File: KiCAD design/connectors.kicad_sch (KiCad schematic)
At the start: 8 parts, among them J201 Conn_02x19_Odd_Even, J202 Conn_01x03_Female, J203 Conn_01x03_Female, J204 Conn_02x19_Odd_Even, J205 JST BATTERY, J206 JST SENS TOF 2, J207 Conn_01x06_Female, J208 JST SENS TOF 1

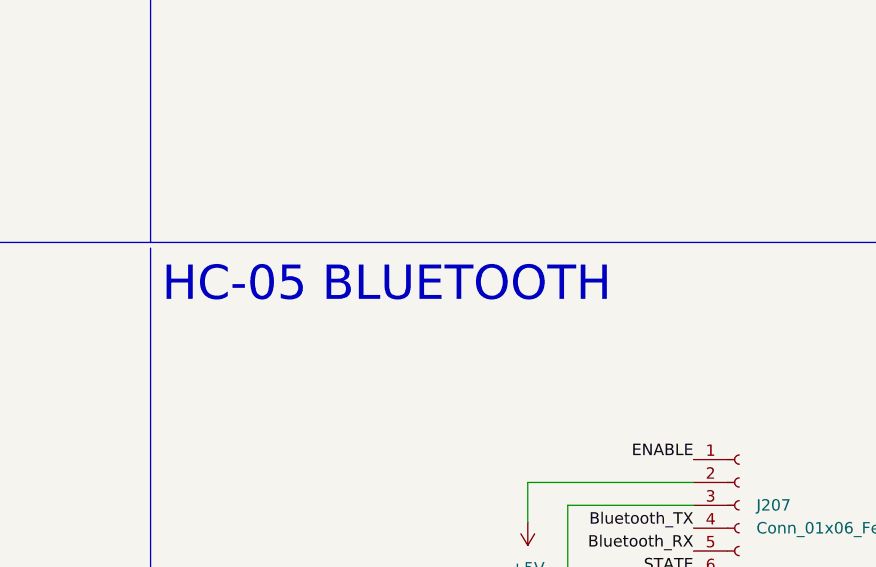
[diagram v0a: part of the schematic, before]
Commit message: add some comments, connector for battery, bluetooth (is now the PMOD BLE from digikey)
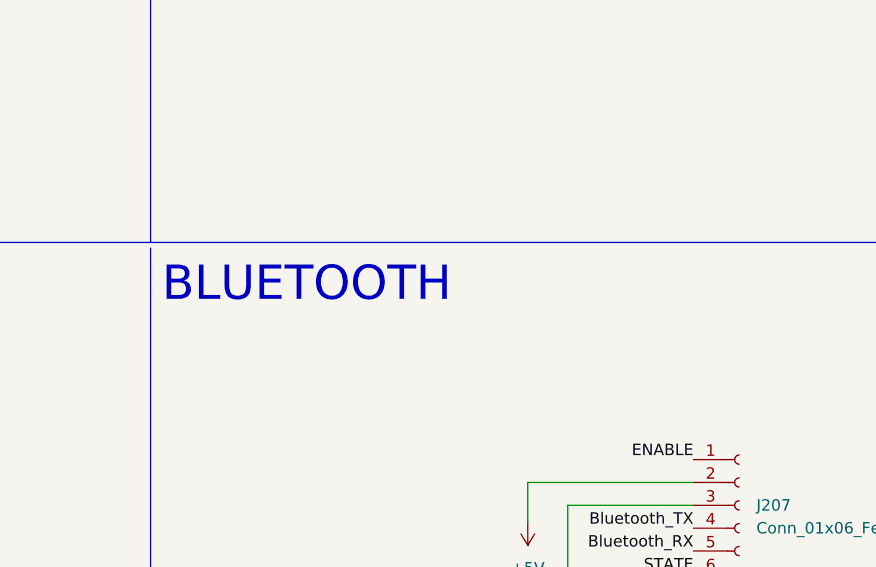
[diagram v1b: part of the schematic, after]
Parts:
- J205: Price (none) -> 1.5; PurchaseLoc (none) -> https://www.digikey.fi/en/products/detail/sparkfun-electron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
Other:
- note added: "BLUETOOTH"
- note removed: "HC-05 BLUETOOTH"
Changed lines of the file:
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@@
     (effects (font (size 4 4)) (justify left bottom))
   )
-  (text "HC-05 BLUETOOTH\n" (at 161.29 116.205 0)
+  (text "BLUETOOTH\n" (at 161.29 116.205 0)
     (effects (font (size 3.81 3.81)) (justify left bottom))
   )
@@
       (effects (font (size 1.27 1.27)) hide)
     )
+    (property "PurchaseLoc" "https://www.digikey.fi/en/products/detail/sparkfun-electronics/PRT-10474/8258064" (id 4) (at 134.62 149.225 0)
+      (effects (font (size 1.27 1.27)) hide)
+    )
+    (property "Price" "1.5" (id 5) (at 134.62 149.225 0)
+      (effects (font (size 1.27 1.27)) hide)
+    )

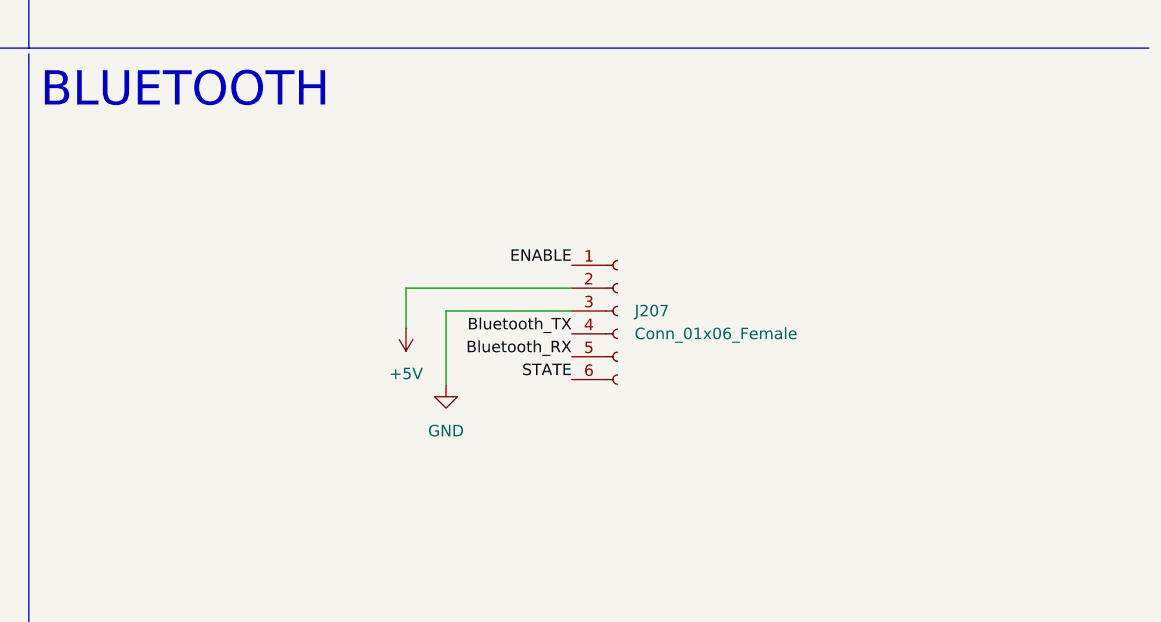
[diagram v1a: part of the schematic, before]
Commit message: add connector for Pmod BLE (HC05 connector still left)
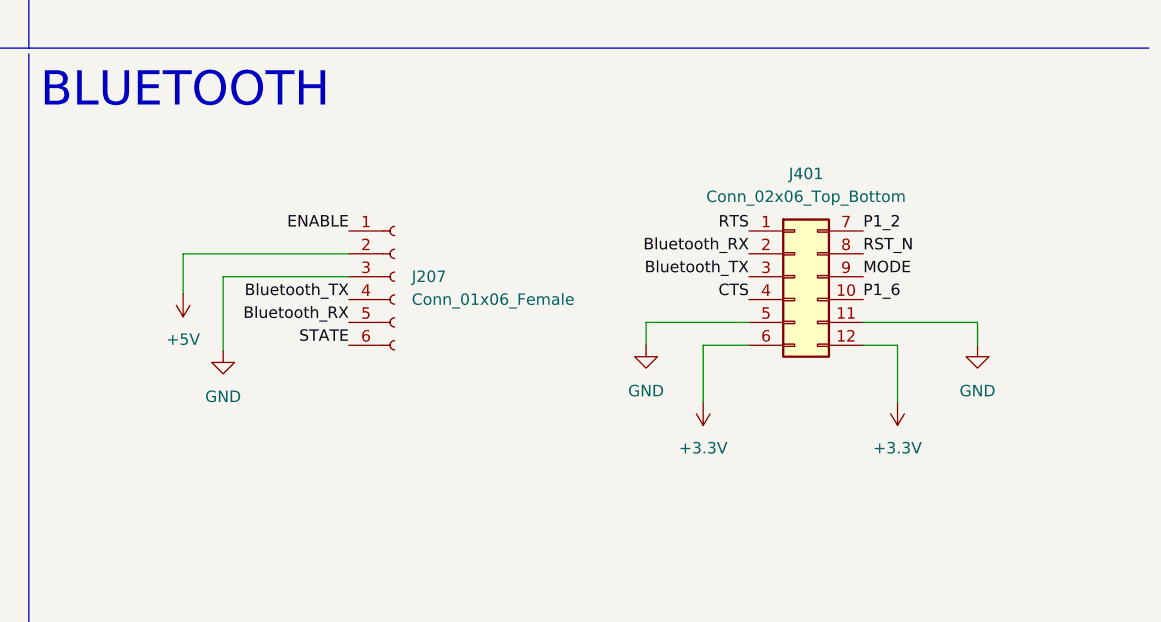
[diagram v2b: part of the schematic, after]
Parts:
- added J401: Conn_02x06_Top_Bottom, symbol Connector_Generic:Conn_02x06_Top_Bottom
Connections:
- net Bluetooth_RX: now also J401.2 (Pin_2)
- net Bluetooth_TX: now also J401.3 (Pin_3)
- net GND: now also J401.11 (Pin_11), J401.5 (Pin_5)
- new net +3.3V: J401.12 (Pin_12), J401.6 (Pin_6)
- new net CTS: J401.4 (Pin_4)
- new net MODE: J401.9 (Pin_9)
- new net P1_2: J401.7 (Pin_7)
- new net P1_6: J401.10 (Pin_10)
- new net RST_N: J401.8 (Pin_8)
- new net RTS: J401.1 (Pin_1)
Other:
- moved on the sheet: J207

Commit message: add comment for bluetooth connectors
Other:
- note added: "Left connector is now HC05, right side is Pmod BLE. We need to delete the other once we know which we will use."
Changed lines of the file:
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@@
     (effects (font (size 3.81 3.81)) (justify left bottom))
+  )
+  (text "Left connector is now HC05, right side is Pmod BLE.\nWe need to delete the other once we know which we will use."
+    (at 191.77 158.75 0)
+    (effects (font (size 1.27 1.27)) (justify left bottom))
   )
   (label "BOOT0" (at 38.1 40.64 180)

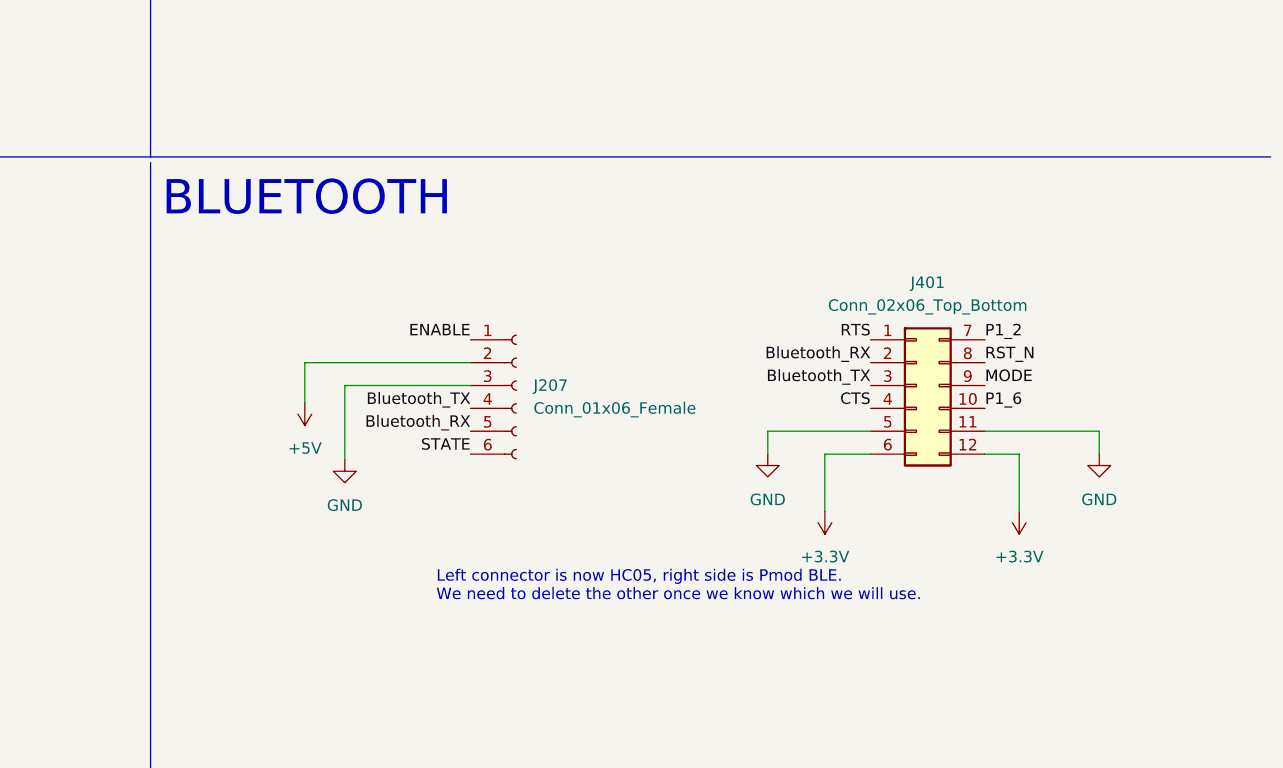
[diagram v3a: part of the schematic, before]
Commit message: remove hc05 connector
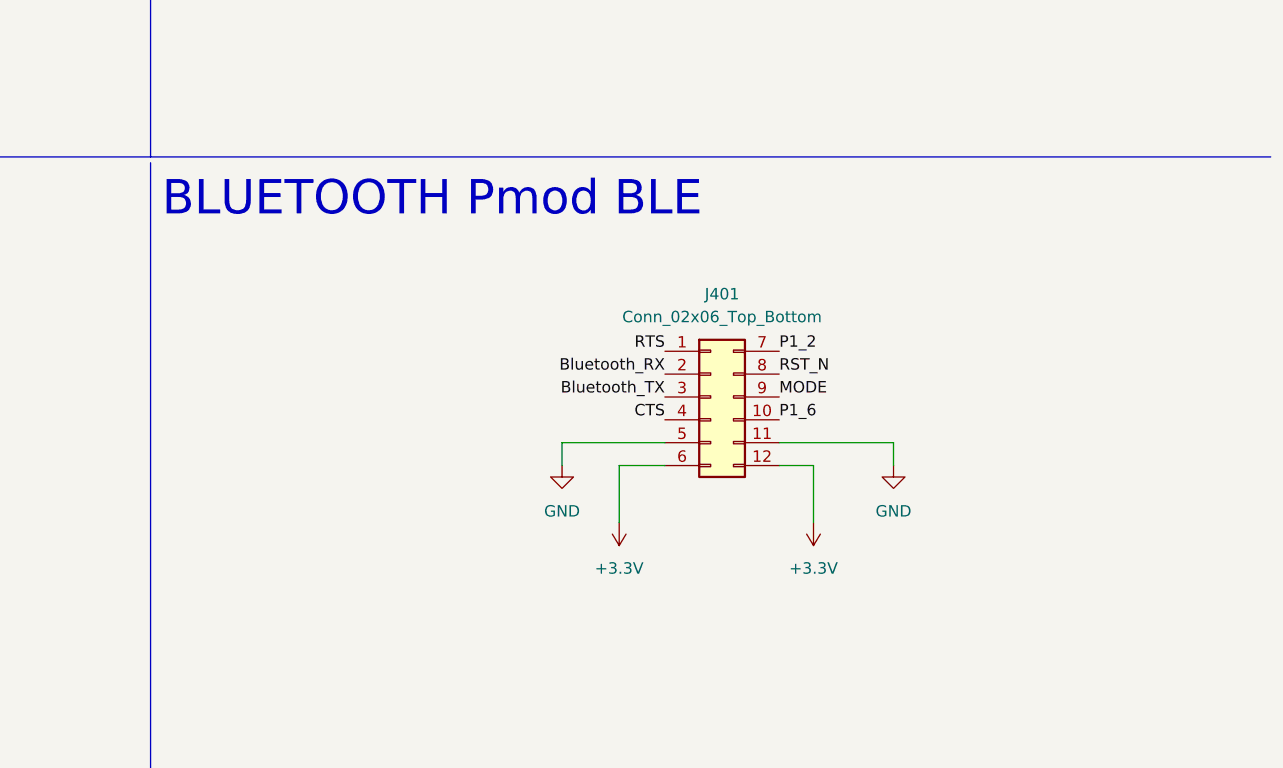
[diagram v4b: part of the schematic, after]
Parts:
- removed J207: Conn_01x06_Female, Connector_JST:JST_XH_B6B-XH-A_1x06_P2.50mm_Vertical, symbol Connector:Conn_01x06_Female
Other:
- note added: "BLUETOOTH Pmod BLE"
- note removed: "BLUETOOTH"
- note removed: "Left connector is now HC05, right side is Pmod BLE. We need to delete the other once we know which we will use."
- moved on the sheet: J401

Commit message: Fixes
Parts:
- J201, J204: footprint Connector_JST:JST_PUD_B38B-PUDSS_2x19_P2.00mm_Vertical -> Connector_PinHeader_2.54mm:PinHeader_2x19_P2.54mm_Vertical
- J202, J203: footprint Connector_JST:JST_XH_B3B-XH-A_1x03_P2.50mm_Vertical -> Connector_JST:JST_EH_B3B-EH-A_1x03_P2.50mm_Vertical
- J206, J208: footprint Connector_JST:JST_XH_B6B-XH-A_1x06_P2.50mm_Vertical -> Connector_PinHeader_2.54mm:PinHeader_1x06_P2.54mm_Vertical
- J401: footprint (none) -> Connector_PinHeader_2.54mm:PinHeader_2x06_P2.54mm_Vertical
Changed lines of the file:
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@@
       (effects (font (size 1.27 1.27)) (justify left))
     )
-    (property "Footprint" "Connector_JST:JST_XH_B3B-XH-A_1x03_P2.50mm_Vertical" (id 2) (at 66.04 157.48 0)
+    (property "Footprint" "Connector_JST:JST_EH_B3B-EH-A_1x03_P2.50mm_Vertical" (id 2) (at 66.04 157.48 0)
       (effects (font (size 1.27 1.27)) hide)
     )
@@
   (symbol (lib_id "Connector_Generic:Conn_02x19_Odd_Even") (at 111.76 55.88 0) (unit 1)
     (in_bom yes) (on_board yes) (fields_autoplaced)
-    (property "Reference" "J204" (id 0) (at 113.03 26.1112 0))
-    (property "Value" "Conn_02x19_Odd_Even" (id 1) (at 113.03 28.6512 0))
-    (property "Footprint" "Connector_JST:JST_PUD_B38B-PUDSS_2x19_P2.00mm_Vertical" (id 2) (at 111.76 55.88 0)
+    (property "Reference" "J204" (id 0) (at 113.03 26.67 0))
+    (property "Value" "Conn_02x19_Odd_Even" (id 1) (at 113.03 29.21 0))
+    (property "Footprint" "Connector_PinHeader_2.54mm:PinHeader_2x19_P2.54mm_Vertical" (id 2) (at 111.76 55.88 0)
       (effects (font (size 1.27 1.27)) hide)
     )
@@
       (effects (font (size 1.27 1.27)) (justify left))
     )
-    (property "Footprint" "Connector_JST:JST_XH_B6B-XH-A_1x06_P2.50mm_Vertical" (id 2) (at 203.2 58.42 0)
+    (property "Footprint" "Connector_PinHeader_2.54mm:PinHeader_1x06_P2.54mm_Vertical" (id 2) (at 203.2 58.42 0)
       (effects (font (size 1.27 1.27)) hide)
     )
@@
   (symbol (lib_id "Connector_Generic:Conn_02x19_Odd_Even") (at 43.18 55.88 0) (unit 1)
     (in_bom yes) (on_board yes) (fields_autoplaced)
-    (property "Reference" "J201" (id 0) (at 44.45 26.1112 0))
-    (property "Value" "Conn_02x19_Odd_Even" (id 1) (at 44.45 28.6512 0))
-    (property "Footprint" "Connector_JST:JST_PUD_B38B-PUDSS_2x19_P2.00mm_Vertical" (id 2) (at 43.18 55.88 0)
+    (property "Reference" "J201" (id 0) (at 44.45 26.67 0))
+    (property "Value" "Conn_02x19_Odd_Even" (id 1) (at 44.45 29.21 0))
+    (property "Footprint" "Connector_PinHeader_2.54mm:PinHeader_2x19_P2.54mm_Vertical" (id 2) (at 43.18 55.88 0)
       (effects (font (size 1.27 1.27)) hide)
     )
@@
       (effects (font (size 1.27 1.27)) (justify left))
     )
-    (property "Footprint" "Connector_JST:JST_XH_B6B-XH-A_1x06_P2.50mm_Vertical" (id 2) (at 257.175 59.055 0)
+    (property "Footprint" "Connector_PinHeader_2.54mm:PinHeader_1x06_P2.54mm_Vertical" (id 2) (at 257.175 59.055 0)
       (effects (font (size 1.27 1.27)) hide)
     )
@@
       (effects (font (size 1.27 1.27)) (justify left))
     )
-    (property "Footprint" "Connector_JST:JST_XH_B3B-XH-A_1x03_P2.50mm_Vertical" (id 2) (at 66.04 137.16 0)
+    (property "Footprint" "Connector_JST:JST_EH_B3B-EH-A_1x03_P2.50mm_Vertical" (id 2) (at 66.04 137.16 0)
       (effects (font (size 1.27 1.27)) hide)
     )
@@
     (property "Reference" "J401" (id 0) (at 223.52 124.46 0))
     (property "Value" "Conn_02x06_Top_Bottom" (id 1) (at 223.52 127 0))
-    (property "Footprint" "" (id 2) (at 222.25 135.89 0)
-      (effects (font (size 1.27 1.27)) hide)
-    )
+    (property "Footprint" "Connector_PinHeader_2.54mm:PinHeader_2x06_P2.54mm_Vertical" (id 2) (at 222.25 135.89 0)
+      (effects (font (size 1.27 1.27)) hide)
+    )

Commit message: more comments (no changes in functionality)
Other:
- note added: "Connector for the Pmod BLE bluetooth module."
- note added: "These connectors are used to connect the Dynamixel AX-12A servomotors into the PCB. A total of five motors will be used, four of which are daisy-chained, thus the need for two molex connectors."
- note added: "These connectors are used to connect the PCB into the Nucleo ST Morpho connectors."
- note added: "These connectors are used to connect the TOF sensors to the PCB. Since the TOF connectors wont be directly mounted on the PCB, they will connect to the connectors via cables."
- note added: "XT60 connector for the LiPo 3S battery"
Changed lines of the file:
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@@
     (effects (font (size 3.81 3.81)) (justify left bottom))
+  )
+  (text "Connector for the Pmod BLE bluetooth module." (at 175.26 161.29 0)
+    (effects (font (size 1.27 1.27)) (justify left bottom))
+  )
+  (text "These connectors are used to connect the Dynamixel AX-12A servomotors into the PCB.\nA total of five motors will be used, four of which are daisy-chained,\nthus the need for two molex connectors."
+    (at 13.97 181.61 0)
+    (effects (font (size 1.27 1.27)) (justify left bottom))
   )
   (text "SERVOMOTORS CONNECTORS\n" (at 12.7 116.84 0)
     (effects (font (size 4 4)) (justify left bottom))
   )
+  (text "XT60 connector for the LiPo 3S battery" (at 107.95 168.91 0)
+    (effects (font (size 1.27 1.27)) (justify left bottom))
+  )
+  (text "These connectors are used to connect the PCB into the Nucleo ST Morpho connectors."
+    (at 36.83 91.44 0)
+    (effects (font (size 1.27 1.27)) (justify left bottom))
+  )
+  (text "These connectors are used to connect the TOF sensors to the PCB.\nSince the TOF connectors wont be directly mounted on the PCB, they will connect to the connectors via cables."
+    (at 168.91 91.44 0)
+    (effects (font (size 1.27 1.27)) (justify left bottom))
+  )
   (text "NUCLEO CONNECTORS" (at 12.7 20.32 0)
